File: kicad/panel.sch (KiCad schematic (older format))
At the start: 2 parts

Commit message: Draw schematic
Commit before trying newer version of KiCad
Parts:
- gave numbers to parts that had none: 2
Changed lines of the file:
@@
 LIBS:opto
 LIBS:transistor
+LIBS:conn
 LIBS:RAMPS_plus-cache
 EELAYER 27 0
@@
 $EndDescr
 $Comp
-L LED D?
+L LED D4
 U 1 1 534EE33D
 P 2000 1950
-F 0 "D?" H 2000 2050 50  0000 C CNN
+F 0 "D4" H 2000 2050 50  0000 C CNN
 F 1 "RED" H 2000 1850 50  0000 C CNN
 F 2 "0805" H 2000 1950 60  0000 C CNN
@@
 $EndComp
 $Comp
-L R R?
+L R R23
 U 1 1 534EE343
 P 2000 1400
-F 0 "R?" V 2080 1400 40  0000 C CNN
+F 0 "R23" V 2080 1400 40  0000 C CNN
 F 1 "1k" V 2007 1401 40  0000 C CNN
 F 2 "0603" V 1930 1400 30  0000 C CNN
@@
 	2000 1050 2000 1150
 $Comp
-L GND #PWR?
+L GND #PWR066
 U 1 1 534EE36C
 P 2000 2250
-F 0 "#PWR?" H 2000 2250 30  0001 C CNN
+F 0 "#PWR066" H 2000 2250 30  0001 C CNN
 F 1 "GND" H 2000 2180 30  0001 C CNN
 F 2 "~" H 2000 2250 60  0000 C CNN

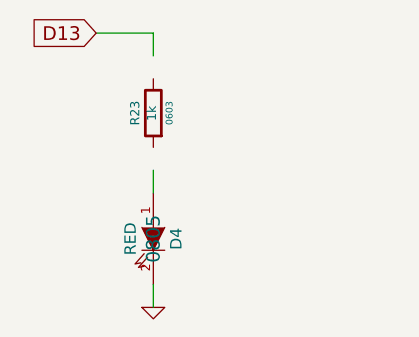
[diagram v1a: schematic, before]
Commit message: Draw schematic
Finished redrawing basic RAMPS schematic

References: #1 #4 #7 #15
Close #5 #17 #18
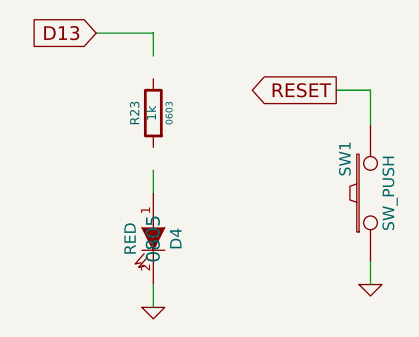
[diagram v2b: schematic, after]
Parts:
- added SW1: SW_PUSH, symbol SW_PUSH
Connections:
- net labels added: RESET
- wire segments 4 -> 7
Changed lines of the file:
@@
 LIBS:transistor
 LIBS:conn
+LIBS:pnConnector
 LIBS:RAMPS_plus-cache
-EELAYER 27 0
+EELAYER 24 0
 EELAYER END
 $Descr A4 11693 8268
@@
 	2000 1050 2000 1150
 $Comp
-L GND #PWR066
+L GND #PWR73
 U 1 1 534EE36C
 P 2000 2250
-F 0 "#PWR066" H 2000 2250 30  0001 C CNN
+F 0 "#PWR73" H 2000 2250 30  0001 C CNN
 F 1 "GND" H 2000 2180 30  0001 C CNN
 F 2 "~" H 2000 2250 60  0000 C CNN
@@
 	1    0    0    -1
 $EndComp
+$Comp
+L SW_PUSH SW1
+U 1 1 536AA4F9
+P 2950 1750
+F 0 "SW1" H 3100 1860 50  0000 C CNN
+F 1 "SW_PUSH" H 2950 1670 50  0000 C CNN
+F 2 "" H 2950 1750 60  0000 C CNN
+F 3 "" H 2950 1750 60  0000 C CNN
+	1    2950 1750
+	0    -1   -1   0
+$EndComp
+$Comp
+L GND #PWR74
+U 1 1 536AA50B
+P 2950 2150
+F 0 "#PWR74" H 2950 2150 30  0001 C CNN
+F 1 "GND" H 2950 2080 30  0001 C CNN
+F 2 "~" H 2950 2150 60  0000 C CNN
+F 3 "~" H 2950 2150 60  0000 C CNN
+	1    2950 2150
+	1    0    0    -1
+$EndComp
+Text GLabel 2800 1300 0    60   Output ~ 0
+RESET
+Wire Wire Line
+	2800 1300 2950 1300
+Wire Wire Line
+	2950 1300 2950 1450
+Wire Wire Line
+	2950 2150 2950 2050
 $EndSCHEMATC

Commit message: Change components to my own
References: #1 #19
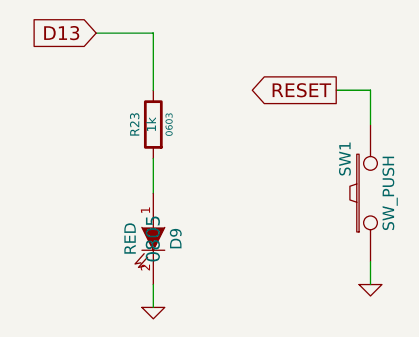
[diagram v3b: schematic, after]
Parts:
- renumbered D4 to D9
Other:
- moved on the sheet: R23
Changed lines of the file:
@@
 LIBS:power
 LIBS:regul
-LIBS:device
 LIBS:opto
-LIBS:transistor
 LIBS:conn
 LIBS:pnConnector
+LIBS:pnRC
+LIBS:pnDiode
+LIBS:pnTransistor
+LIBS:pnSymbols
+LIBS:pnPins
 LIBS:RAMPS_plus-cache
 EELAYER 24 0
@@
 $EndDescr
 $Comp
-L LED D4
+L LED D9
 U 1 1 534EE33D
 P 2000 1950
-F 0 "D4" H 2000 2050 50  0000 C CNN
+F 0 "D9" H 2000 2050 50  0000 C CNN
 F 1 "RED" H 2000 1850 50  0000 C CNN
 F 2 "0805" H 2000 1950 60  0000 C CNN
@@
 L R R23
 U 1 1 534EE343
-P 2000 1400
-F 0 "R23" V 2080 1400 40  0000 C CNN
-F 1 "1k" V 2007 1401 40  0000 C CNN
-F 2 "0603" V 1930 1400 30  0000 C CNN
-F 3 "~" H 2000 1400 30  0000 C CNN
-	1    2000 1400
+P 2000 1450
+F 0 "R23" V 2080 1450 40  0000 C CNN
+F 1 "1k" V 2007 1451 40  0000 C CNN
+F 2 "0603" V 1930 1450 30  0000 C CNN
+F 3 "~" H 2000 1450 30  0000 C CNN
+	1    2000 1450
 	-1   0    0    1
 $EndComp
 Wire Wire Line
-	2000 1750 2000 1650
+	2000 1750 2000 1600
 Wire Wire Line
 	2000 2250 2000 2150
@@
 	1750 1050 2000 1050
 Wire Wire Line
-	2000 1050 2000 1150
+	2000 1050 2000 1300
 $Comp
-L GND #PWR73
+L GND #PWR77
 U 1 1 534EE36C
 P 2000 2250
-F 0 "#PWR73" H 2000 2250 30  0001 C CNN
+F 0 "#PWR77" H 2000 2250 30  0001 C CNN
 F 1 "GND" H 2000 2180 30  0001 C CNN
 F 2 "~" H 2000 2250 60  0000 C CNN
@@
 $EndComp
 $Comp
-L GND #PWR74
+L GND #PWR76
 U 1 1 536AA50B
 P 2950 2150
-F 0 "#PWR74" H 2950 2150 30  0001 C CNN
+F 0 "#PWR76" H 2950 2150 30  0001 C CNN
 F 1 "GND" H 2950 2080 30  0001 C CNN
 F 2 "~" H 2950 2150 60  0000 C CNN

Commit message: Add YZ connector. Add endstop filters.
Close #23
References: #3 #20
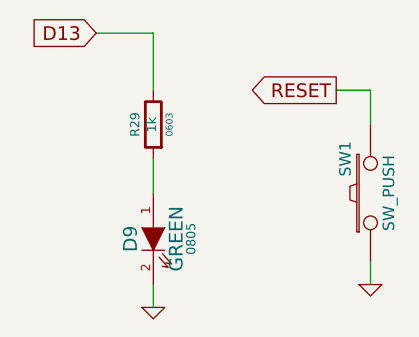
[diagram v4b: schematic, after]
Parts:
- D9: value RED -> GREEN
- renumbered R23 to R29
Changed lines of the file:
@@
 LIBS:pnSymbols
 LIBS:pnPins
+LIBS:pnModules
+LIBS:pnAnalogOther
+LIBS:pnLogic
 LIBS:RAMPS_plus-cache
 EELAYER 24 0
@@
 $EndDescr
 $Comp
-L LED D9
-U 1 1 534EE33D
-P 2000 1950
-F 0 "D9" H 2000 2050 50  0000 C CNN
-F 1 "RED" H 2000 1850 50  0000 C CNN
-F 2 "0805" H 2000 1950 60  0000 C CNN
-F 3 "~" H 2000 1950 60  0000 C CNN
-	1    2000 1950
-	0    1    1    0
-$EndComp
-$Comp
-L R R23
+L R R29
 U 1 1 534EE343
 P 2000 1450
-F 0 "R23" V 2080 1450 40  0000 C CNN
+F 0 "R29" V 2080 1450 40  0000 C CNN
 F 1 "1k" V 2007 1451 40  0000 C CNN
 F 2 "0603" V 1930 1450 30  0000 C CNN
@@
 	2000 1050 2000 1300
 $Comp
-L GND #PWR77
+L GND #PWR066
 U 1 1 534EE36C
 P 2000 2250
-F 0 "#PWR77" H 2000 2250 30  0001 C CNN
+F 0 "#PWR066" H 2000 2250 30  0001 C CNN
 F 1 "GND" H 2000 2180 30  0001 C CNN
 F 2 "~" H 2000 2250 60  0000 C CNN
@@
 $EndComp
 $Comp
-L GND #PWR76
+L GND #PWR067
 U 1 1 536AA50B
 P 2950 2150
-F 0 "#PWR76" H 2950 2150 30  0001 C CNN
+F 0 "#PWR067" H 2950 2150 30  0001 C CNN
 F 1 "GND" H 2950 2080 30  0001 C CNN
 F 2 "~" H 2950 2150 60  0000 C CNN
@@
 Wire Wire Line
 	2950 2150 2950 2050
+$Comp
+L LED D9
+U 1 1 536FE241
+P 2000 1950
+F 0 "D9" H 2000 2050 60  0000 C CNN
+F 1 "GREEN" H 2000 1850 60  0000 C CNN
+F 2 "0805" H 2000 1785 40  0000 C CNN
+F 3 "~" H 2000 1950 60  0000 C CNN
+	1    2000 1950
+	0    -1   1    0
+$EndComp
 $EndSCHEMATC

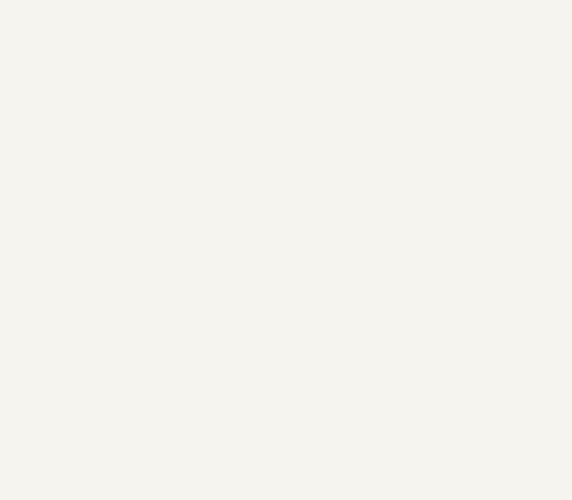
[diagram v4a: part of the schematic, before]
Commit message: Add panel connectors. Minor ERC fixes.
References: #11
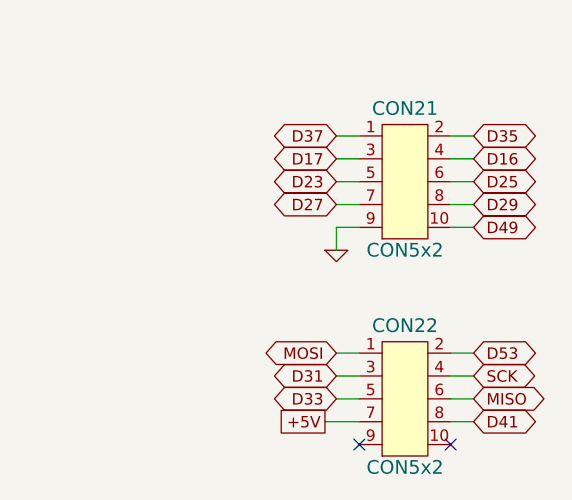
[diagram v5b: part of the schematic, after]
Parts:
- added CON21, CON22: CON5x2, symbol CON5x2
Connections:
- net GND: now also CON21.9
- new net +5V: CON22.7
- new net D16: CON21.4
- new net D17: CON21.3
- new net D23: CON21.5
- new net D25: CON21.6
- new net D27: CON21.7
- new net D29: CON21.8
- new net D31: CON22.3
- new net D33: CON22.5
- new net D35: CON21.2
- new net D37: CON21.1
- new net D41: CON22.8
- new net D49: CON21.10
- new net D53: CON22.2
- new net MISO: CON22.6
- new net MOSI: CON22.1
- new net SCK: CON22.4
- no-connect marks 0 -> 2
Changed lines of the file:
@@
 	-1   0    0    1
 $EndComp
-Wire Wire Line
-	2000 1750 2000 1600
-Wire Wire Line
-	2000 2250 2000 2150
 Text GLabel 1750 1050 0    60   Input ~ 0
 D13
-Wire Wire Line
-	1750 1050 2000 1050
-Wire Wire Line
-	2000 1050 2000 1300
 $Comp
-L GND #PWR066
+L GND #PWR064
 U 1 1 534EE36C
 P 2000 2250
-F 0 "#PWR066" H 2000 2250 30  0001 C CNN
+F 0 "#PWR064" H 2000 2250 30  0001 C CNN
 F 1 "GND" H 2000 2180 30  0001 C CNN
 F 2 "~" H 2000 2250 60  0000 C CNN
@@
 $EndComp
 $Comp
-L GND #PWR067
+L GND #PWR065
 U 1 1 536AA50B
 P 2950 2150
-F 0 "#PWR067" H 2950 2150 30  0001 C CNN
+F 0 "#PWR065" H 2950 2150 30  0001 C CNN
 F 1 "GND" H 2950 2080 30  0001 C CNN
 F 2 "~" H 2950 2150 60  0000 C CNN
@@
 Text GLabel 2800 1300 0    60   Output ~ 0
 RESET
-Wire Wire Line
-	2800 1300 2950 1300
-Wire Wire Line
-	2950 1300 2950 1450
-Wire Wire Line
-	2950 2150 2950 2050
 $Comp
 L LED D9
@@
 	0    -1   1    0
 $EndComp
+Text GLabel 6150 1500 2    50   BiDi ~ 0
+D35
+Text GLabel 5550 1500 0    50   BiDi ~ 0
+D37
+$Comp
+L CON5x2 CON21
+U 1 1 538CD96D
+P 5850 1700
+F 0 "CON21" H 5850 2020 60  0000 C CNN
+F 1 "CON5x2" H 5850 1400 60  0000 C CNN
+F 2 "" H 5850 1700 40  0000 C CNN
+F 3 "" H 5850 1700 40  0000 C CNN
+	1    5850 1700
+	1    0    0    -1
+$EndComp
+$Comp
+L CON5x2 CON22
+U 1 1 538CD9E6
+P 5850 2650
+F 0 "CON22" H 5850 2970 60  0000 C CNN
+F 1 "CON5x2" H 5850 2350 60  0000 C CNN
+F 2 "" H 5850 2650 40  0000 C CNN
+F 3 "" H 5850 2650 40  0000 C CNN
+	1    5850 2650
+	1    0    0    -1
+$EndComp
+Text GLabel 5550 1600 0    50   BiDi ~ 0
+D17
+Text GLabel 5550 1700 0    50   BiDi ~ 0
+D23
+Text GLabel 5550 1800 0    50   BiDi ~ 0
+D27
+Text GLabel 6150 1600 2    50   BiDi ~ 0
+D16
+Text GLabel 6150 1700 2    50   BiDi ~ 0
+D25
+Text GLabel 6150 1800 2    50   BiDi ~ 0
+D29
+Text GLabel 6150 1900 2    50   BiDi ~ 0
+D49
+Wire Wire Line
+	2000 1750 2000 1600
+Wire Wire Line
+	2000 2250 2000 2150
+Wire Wire Line
+	1750 1050 2000 1050
+Wire Wire Line
+	2000 1050 2000 1300
+Wire Wire Line
+	2800 1300 2950 1300
+Wire Wire Line
+	2950 1300 2950 1450
+Wire Wire Line
+	2950 2150 2950 2050
+Wire Wire Line
+	6150 1500 6050 1500
+Wire Wire Line
+	6050 1600 6150 1600
+Wire Wire Line
+	6150 1700 6050 1700
+Wire Wire Line
+	6050 1800 6150 1800
+Wire Wire Line
+	6150 1900 6050 1900
+Wire Wire Line
+	5550 1900 5650 1900
+Wire Wire Line
+	5550 1800 5650 1800
+Wire Wire Line
+	5550 1700 5650 1700
+Wire Wire Line
+	5650 1600 5550 1600
+Wire Wire Line
+	5650 1500 5550 1500
+$Comp
+L GND #PWR066
+U 1 1 538CDD99
+P 5550 2000
+F 0 "#PWR066" H 5550 2000 30  0001 C CNN
+F 1 "GND" H 5550 1930 30  0001 C CNN
+F 2 "~" H 5550 2000 60  0000 C CNN
+F 3 "~" H 5550 2000 60  0000 C CNN
+	1    5550 2000
+	1    0    0    -1
+$EndComp
+Wire Wire Line
+	5550 1900 5550 2000
+Text GLabel 5550 2450 0    50   BiDi ~ 0
+MOSI
+Text GLabel 5550 2550 0    50   BiDi ~ 0
+D31
+Text GLabel 5550 2650 0    50   BiDi ~ 0
+D33
+Text GLabel 5500 2750 0    50   UnSpc ~ 0
++5V
+Wire Wire Line
+	5500 2750 5650 2750
+Wire Wire Line
+	5550 2650 5650 2650
+Wire Wire Line
+	5650 2550 5550 2550
+Wire Wire Line
+	5650 2450 5550 2450
+Text GLabel 6150 2450 2    50   BiDi ~ 0
+D53
+Text GLabel 6150 2550 2    50   BiDi ~ 0
+SCK
+Text GLabel 6150 2650 2    50   BiDi ~ 0
+MISO
+Text GLabel 6150 2750 2    50   BiDi ~ 0
+D41
+Wire Wire Line
+	6150 2450 6050 2450
+Wire Wire Line
+	6050 2550 6150 2550
+Wire Wire Line
+	6150 2650 6050 2650
+Wire Wire Line
+	6050 2750 6150 2750
+NoConn ~ 6050 2850
+NoConn ~ 5650 2850
 $EndSCHEMATC

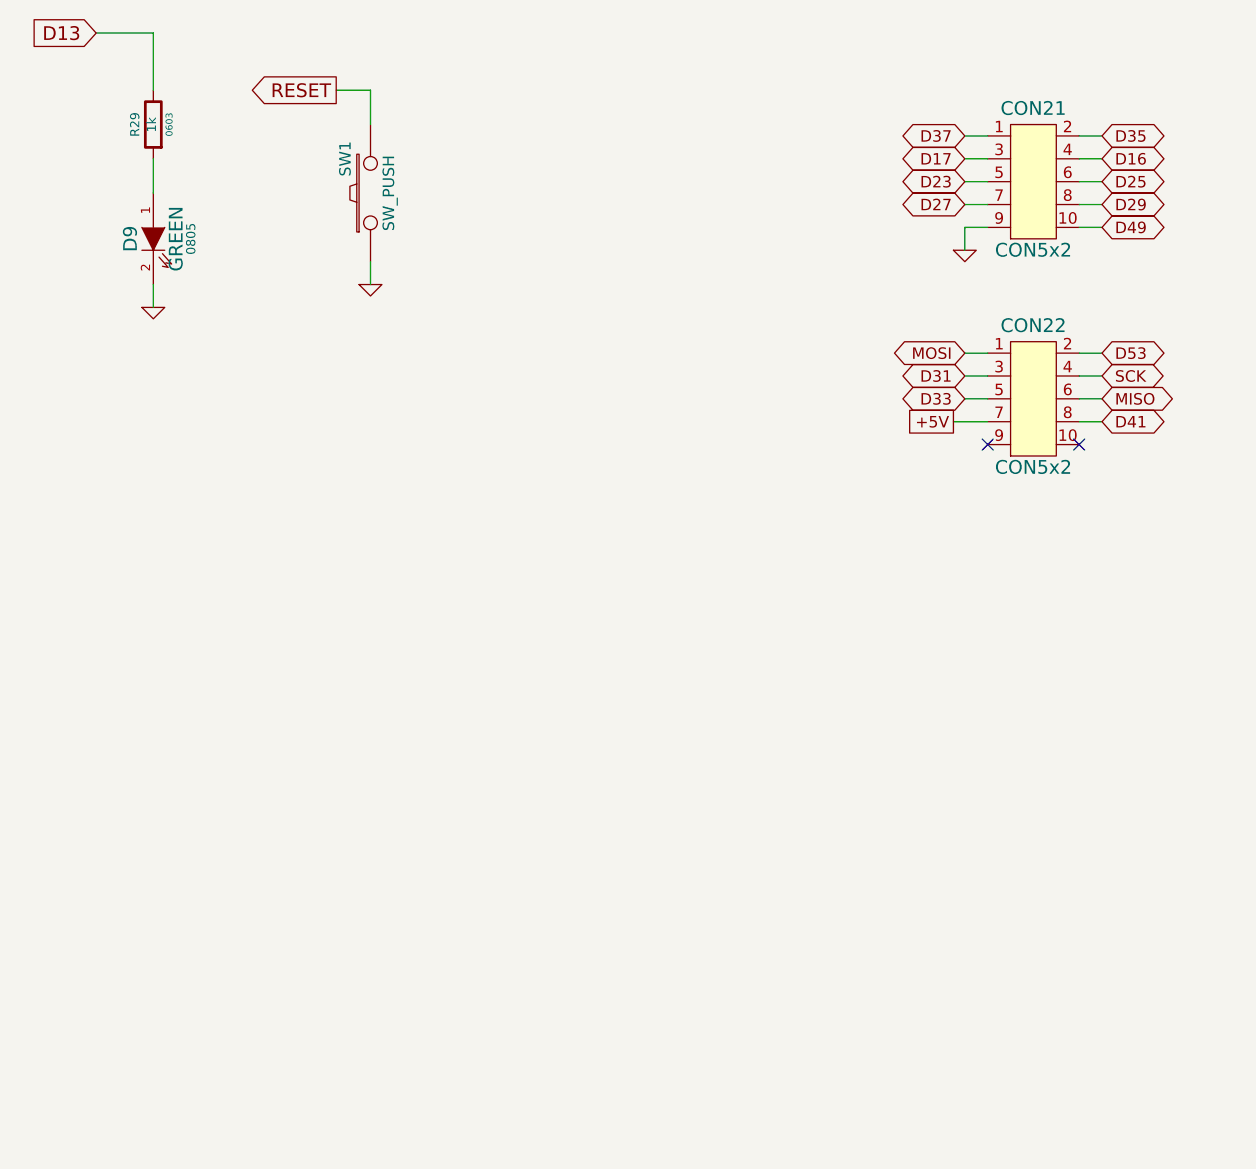
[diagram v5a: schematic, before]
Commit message: Change CD40109 to CD4504
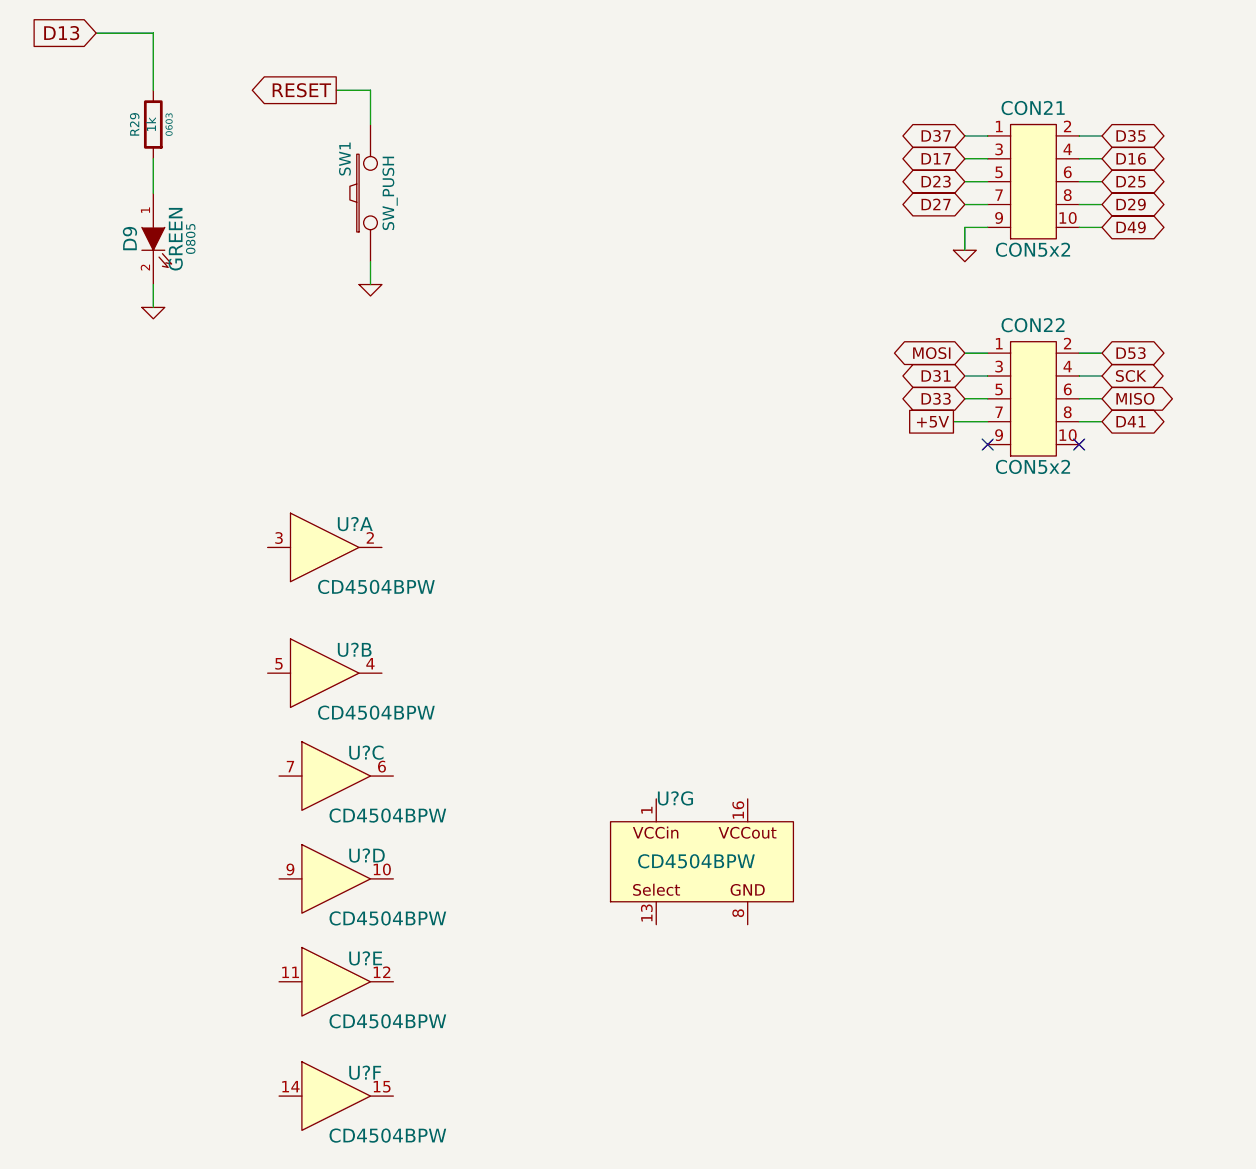
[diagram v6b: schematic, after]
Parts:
- added U? (x7): CD4504BPW, TSSOP16, symbol CD4504BPW
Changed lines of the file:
@@
 D13
 $Comp
-L GND #PWR064
+L GND #PWR54
 U 1 1 534EE36C
 P 2000 2250
-F 0 "#PWR064" H 2000 2250 30  0001 C CNN
+F 0 "#PWR54" H 2000 2250 30  0001 C CNN
 F 1 "GND" H 2000 2180 30  0001 C CNN
 F 2 "~" H 2000 2250 60  0000 C CNN
@@
 $EndComp
 $Comp
-L GND #PWR065
+L GND #PWR53
 U 1 1 536AA50B
 P 2950 2150
-F 0 "#PWR065" H 2950 2150 30  0001 C CNN
+F 0 "#PWR53" H 2950 2150 30  0001 C CNN
 F 1 "GND" H 2950 2080 30  0001 C CNN
 F 2 "~" H 2950 2150 60  0000 C CNN
@@
 	5650 1500 5550 1500
 $Comp
-L GND #PWR066
+L GND #PWR52
 U 1 1 538CDD99
 P 5550 2000
-F 0 "#PWR066" H 5550 2000 30  0001 C CNN
+F 0 "#PWR52" H 5550 2000 30  0001 C CNN
 F 1 "GND" H 5550 1930 30  0001 C CNN
 F 2 "~" H 5550 2000 60  0000 C CNN
@@
 NoConn ~ 6050 2850
 NoConn ~ 5650 2850
+$Comp
+L CD4504BPW U?
+U 1 1 538D7C6B
+P 2750 3300
+F 0 "U?" H 2800 3400 60  0000 L CNN
+F 1 "CD4504BPW" H 2975 3125 60  0000 C CNN
+F 2 "TSSOP16" H 2625 3300 40  0001 L CNN
+F 3 "" H 2600 3900 60  0001 L CNN
+	1    2750 3300
+	1    0    0    -1
+$EndComp
+$Comp
+L CD4504BPW U?
+U 2 1 538D7CB8
+P 2750 3850
+F 0 "U?" H 2800 3950 60  0000 L CNN
+F 1 "CD4504BPW" H 2975 3675 60  0000 C CNN
+F 2 "TSSOP16" H 2625 3850 40  0001 L CNN
+F 3 "" H 2600 4450 60  0001 L CNN
+	2    2750 3850
+	1    0    0    -1
+$EndComp
+$Comp
+L CD4504BPW U?
+U 3 1 538D7D0D
+P 2800 4300
+F 0 "U?" H 2850 4400 60  0000 L CNN
+F 1 "CD4504BPW" H 3025 4125 60  0000 C CNN
+F 2 "TSSOP16" H 2675 4300 40  0001 L CNN
+F 3 "" H 2650 4900 60  0001 L CNN
+	3    2800 4300
+	1    0    0    -1
+$EndComp
+$Comp
+L CD4504BPW U?
+U 4 1 538D7D48
+P 2800 4750
+F 0 "U?" H 2850 4850 60  0000 L CNN
+F 1 "CD4504BPW" H 3025 4575 60  0000 C CNN
+F 2 "TSSOP16" H 2675 4750 40  0001 L CNN
+F 3 "" H 2650 5350 60  0001 L CNN
+	4    2800 4750
+	1    0    0    -1
+$EndComp
+$Comp
+L CD4504BPW U?
+U 5 1 538D7D79
+P 2800 5200
+F 0 "U?" H 2850 5300 60  0000 L CNN
+F 1 "CD4504BPW" H 3025 5025 60  0000 C CNN
+F 2 "TSSOP16" H 2675 5200 40  0001 L CNN
+F 3 "" H 2650 5800 60  0001 L CNN
+	5    2800 5200
+	1    0    0    -1
+$EndComp
+$Comp
+L CD4504BPW U?
+U 6 1 538D7DA4
+P 2800 5700
+F 0 "U?" H 2850 5800 60  0000 L CNN
+F 1 "CD4504BPW" H 3025 5525 60  0000 C CNN
+F 2 "TSSOP16" H 2675 5700 40  0001 L CNN
+F 3 "" H 2650 6300 60  0001 L CNN
+	6    2800 5700
+	1    0    0    -1
+$EndComp
+$Comp
+L CD4504BPW U?
+U 7 1 538D7DD3
+P 4150 4500
+F 0 "U?" H 4200 4600 60  0000 L CNN
+F 1 "CD4504BPW" H 4375 4325 60  0000 C CNN
+F 2 "TSSOP16" H 4025 4500 40  0001 L CNN
+F 3 "" H 4000 5100 60  0001 L CNN
+	7    4150 4500
+	1    0    0    -1
+$EndComp
 $EndSCHEMATC
